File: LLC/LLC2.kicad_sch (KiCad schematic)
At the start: 15 parts, among them T1 Transformer_1P_SS

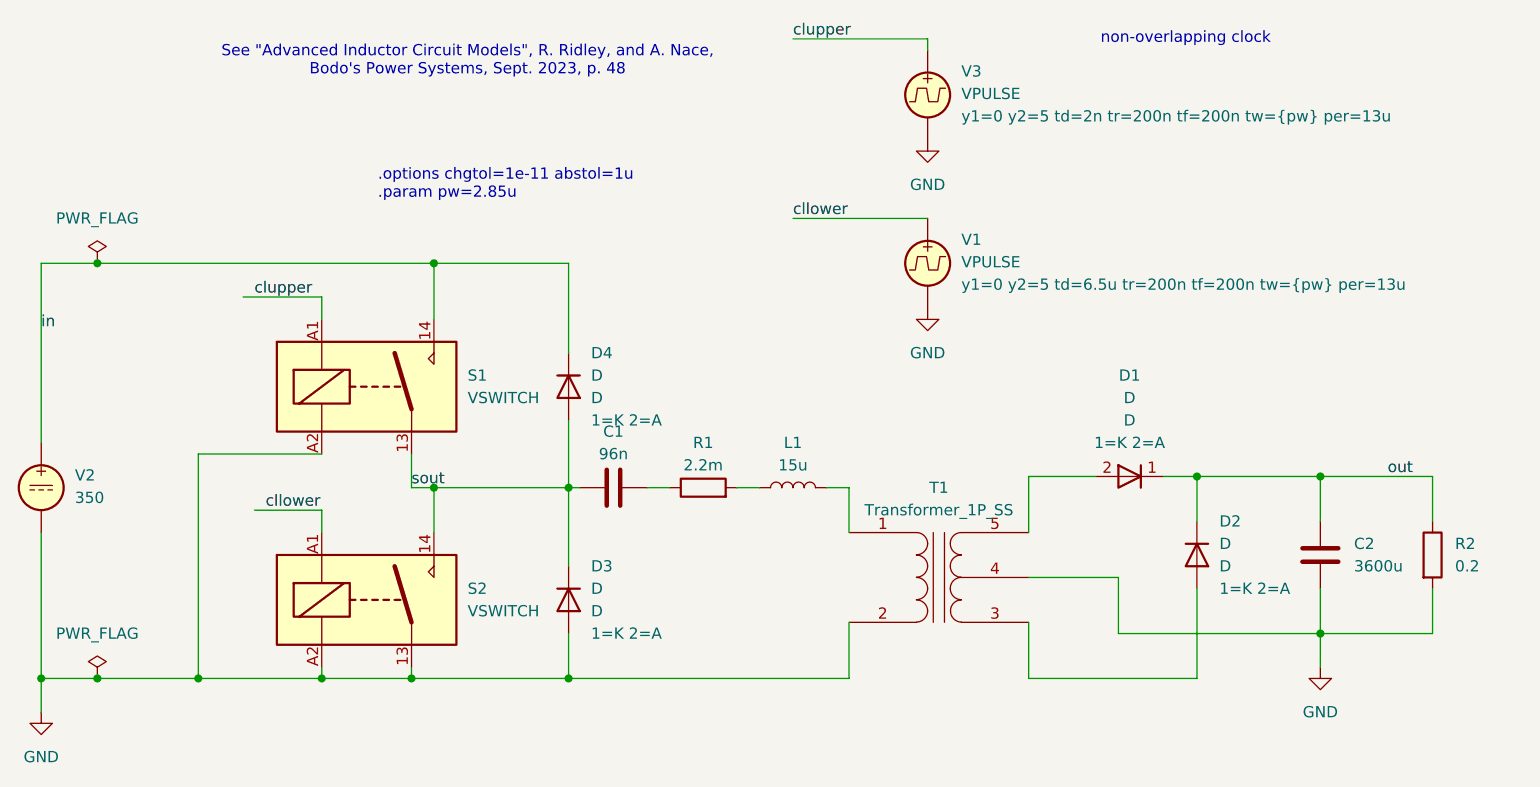
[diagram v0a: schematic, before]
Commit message: Updated LLC analysis files From Holger's examples at https://forum.kicad.info/t/more-simulation-examples-for-kicad-eeschema-ngspice/45546
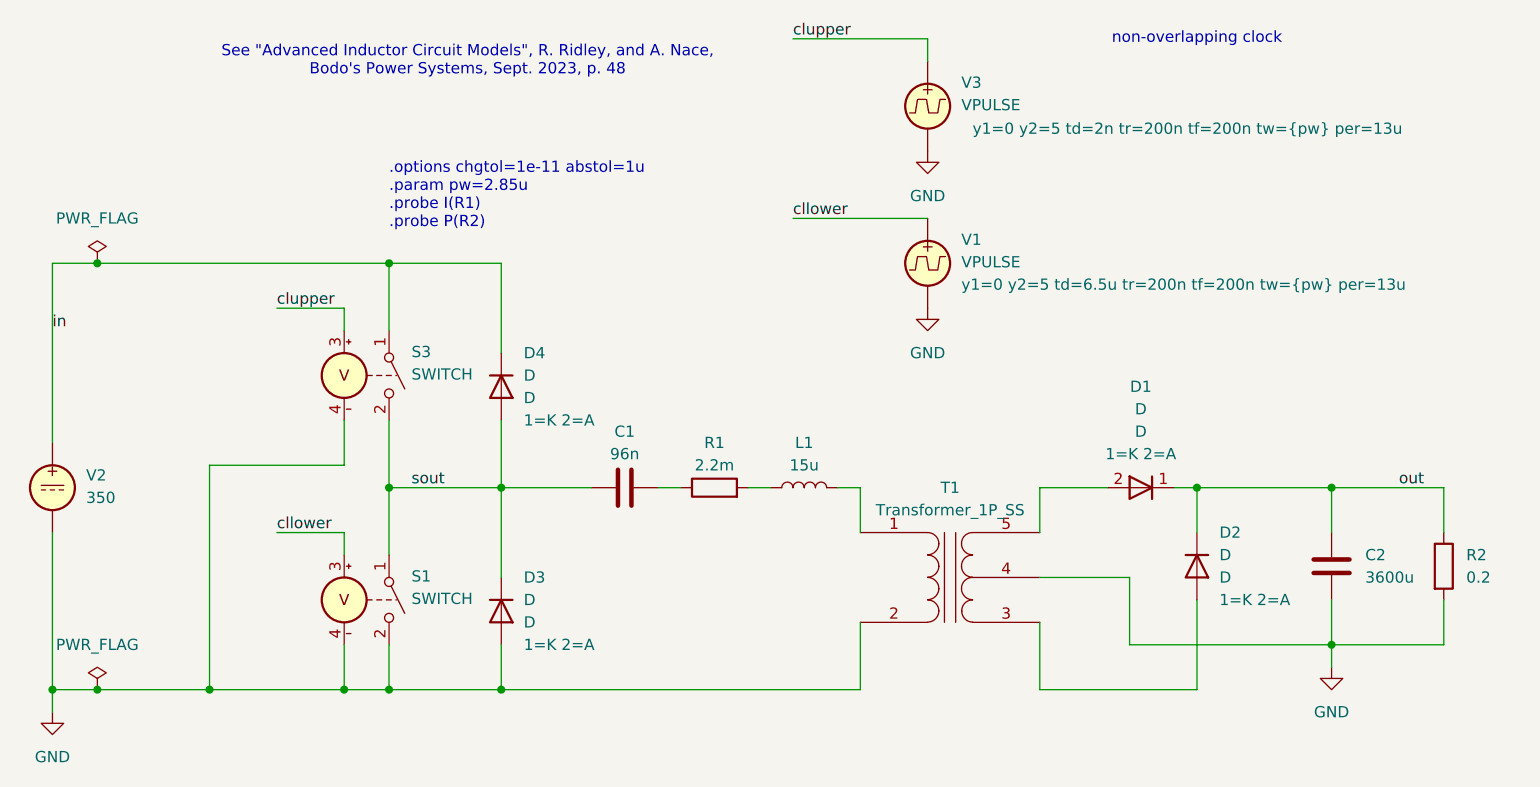
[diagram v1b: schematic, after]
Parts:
- removed S1, S2: VSWITCH, symbol Relay:Relay_SPST-NO
- added S1, S3: SWITCH, symbol Simulation_SPICE:SWITCH
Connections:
- net GND: now also S1.2 (N-), S1.4 (C-), S3.4 (C-)
- net cllower: now also S1.3 (C+)
- net clupper: now also S3.3 (C+)
- net in: now also S3.1 (N+)
- net sout: now also S1.1 (N+), S3.2 (N-)
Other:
- note added: ".options chgtol=1e-11 abstol=1u .param pw=2.85u .probe I(R1) .probe P(R2)"
- note removed: ".options chgtol=1e-11 abstol=1u .param pw=2.85u"
- moved on the sheet: C1, C2, D1, D2, D3, D4, L1, R1, R2, T1, V2, V3
